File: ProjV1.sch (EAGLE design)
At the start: 24 parts, among them IC1 CD4007UBM, IC2 CD4007UBM, IC3 CD4007UBM, U1 MIC5504-3.3YM5-T5, U2 MCP2200-I/SS, U3 ATMEGA328PB-AU, U4 EN11-HSM1BF20, Y1 CSTNE12M0G55A000R0

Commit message: Updated Schematic
Fixed usb, made power source changes, got rid of missing part error relayed out board
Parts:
- removed CN1: (no value), adafruit:USBMINIB
- added R1, R2, R3, R4: 10k, rcl:R-US_R0805
- added T5, T6: (no value), zetex:NMOSSOT23
- added USB1: C77238, usbFromLCSC:C77238
- U2: value MCP2200-I/SS -> MCP2200-I/MQ; device MCP2200-I_SS:MCP2200-I/SS -> MCP2200-I_MQ:MCP2200-I/MQ
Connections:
- net RX/TX renamed N$10
- net TX/RX renamed N$11
- removed net N$8: CN1.ID
- new net N$16: R2.1, T5.S, U$1.SDA
- new net N$19: R4.1, T6.S, U$1.SCL
- new net N$7: C1.1, U2.VUSB
- net +3V3: now also R2.2, R4.2, T5.G, T6.G; no longer C1.1, ISP1.VCC, U2.VDD, U2.VUSB, U3.AVCC, U3.VCC
- net +5V: now also ISP1.VCC, R1.2, R3.2, U2.VDD, U3.AVCC, U3.VCC, USB1.VBUS; no longer CN1.VBUS
- net 0: now also U2.!RST, U2.EXP, USB1.GND, USB1.SHEILD1, USB1.SHEILD2, USB1.SHEILD3, USB1.SHEILD4; no longer CN1.GND
- net C4: now also IC2.Q2_(N)_DRAIN, IC2.Q2_(P)_DRAIN; no longer IC2.Q1_(N)_DRAIN, IC2.Q1_(P)_SOURCE
- net C5: now also IC2.Q1_(N)_DRAIN, IC2.Q1_(P)_SOURCE; no longer IC2.Q2_(N)_DRAIN, IC2.Q2_(P)_DRAIN
- net D+: now also U2.GP6/RXLED, USB1.D+; no longer CN1.D+, U2.D+
- net D-: now also U2.GP7/TXLED, USB1.D-; no longer CN1.D-, U2.D-
- net LC4: now also IC2.Q2_GATES; no longer IC2.Q1_GATES
- net LC5: now also IC2.Q1_GATES; no longer IC2.Q2_GATES
- net SCL: now also R3.1, T6.D; no longer U$1.SCL
- net SDA: now also R1.1, T5.D; no longer U$1.SDA
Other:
- moved on the sheet: C1, T1, T2, T3, T4

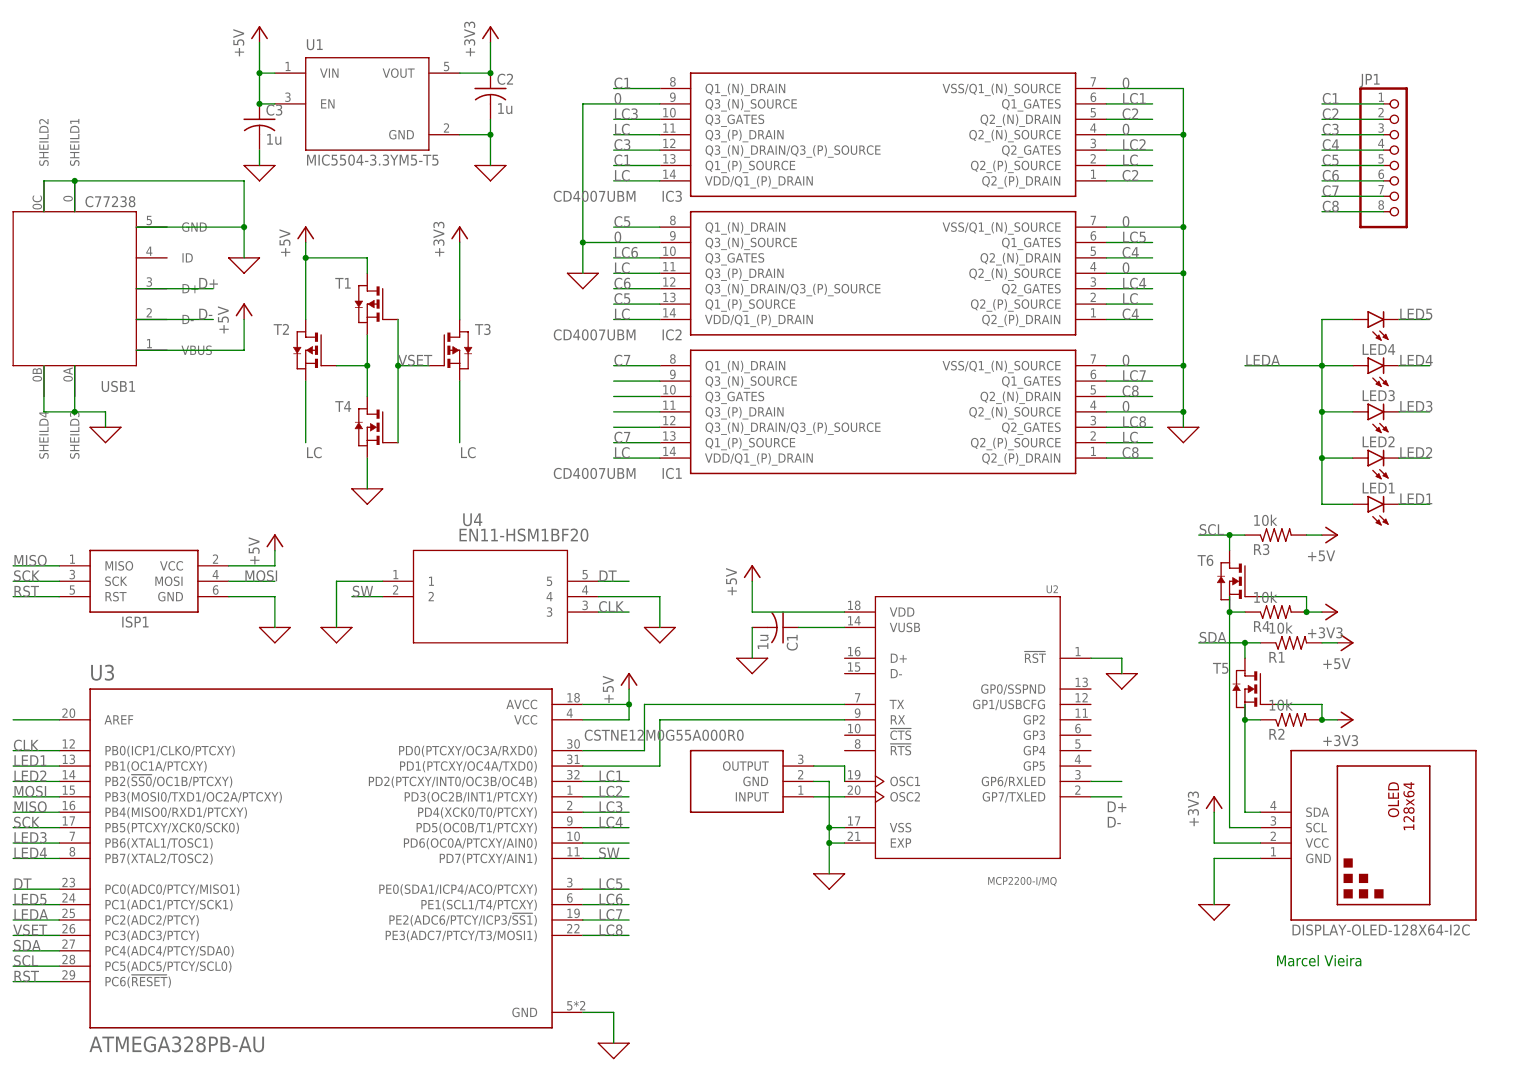
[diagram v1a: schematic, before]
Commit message: Added copies of old versions
Updated version numbers and add old versions for comparison and report writing
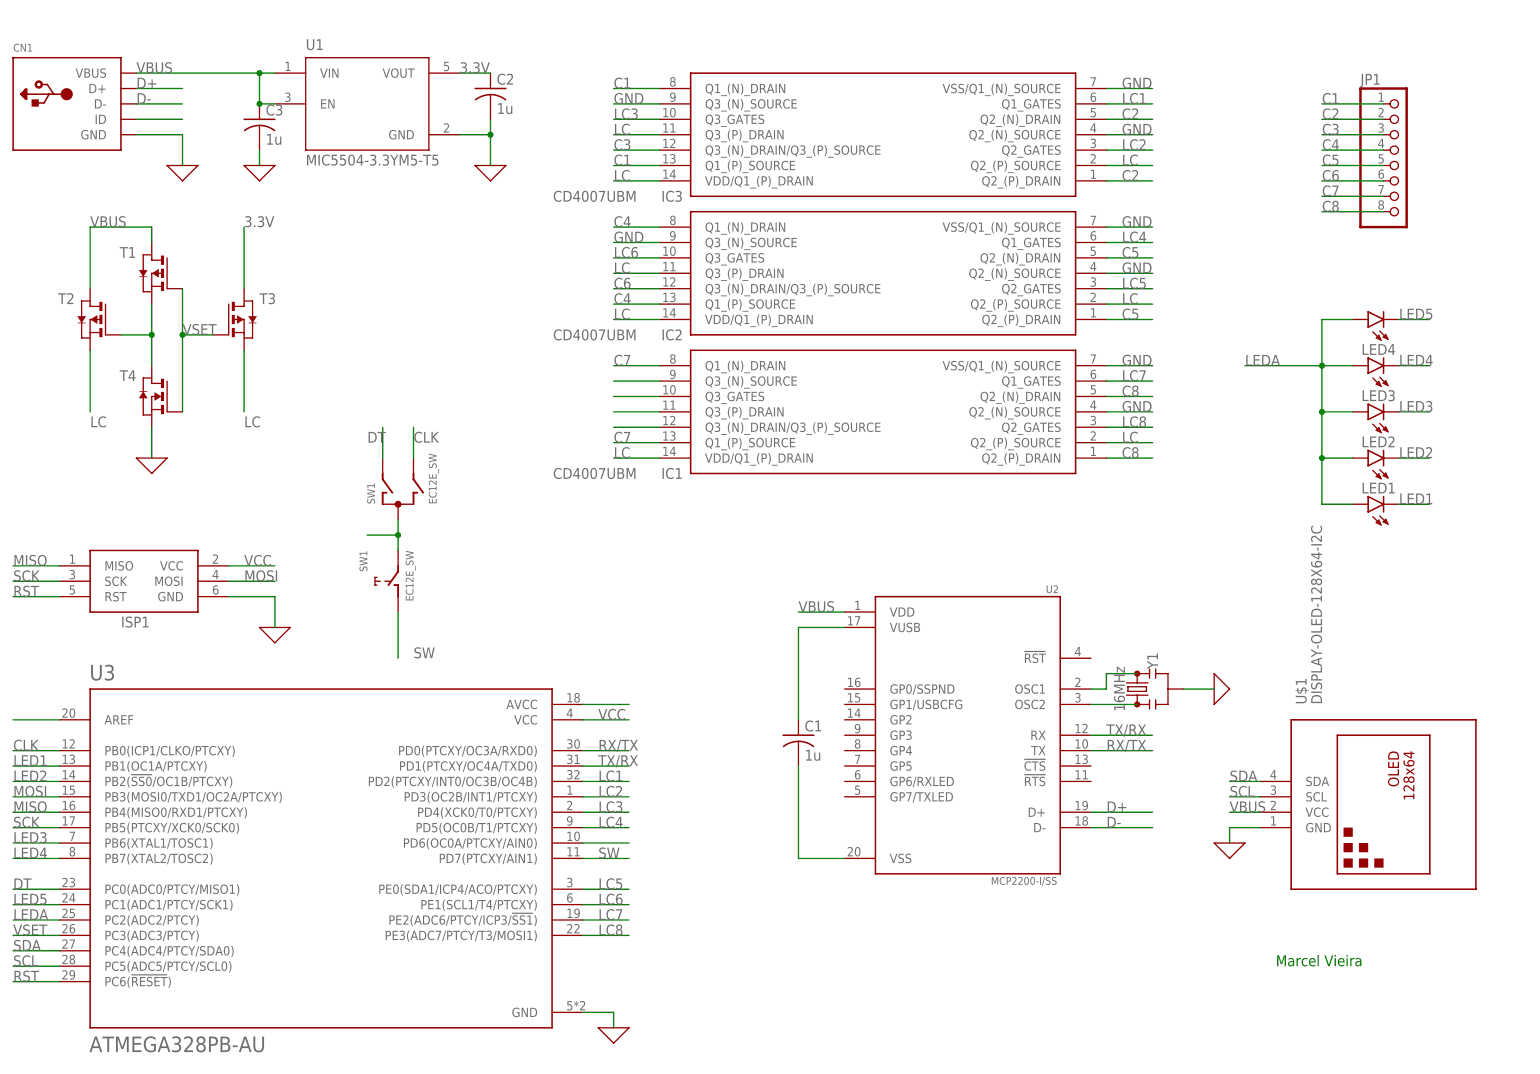
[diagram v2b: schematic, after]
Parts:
- removed R1, R2, R3, R4: 10k, rcl:R-US_R0805
- removed T5, T6: (no value), zetex:NMOSSOT23
- removed U4: EN11-HSM1BF20, EN11-HSM1BF20:EN11-HSM1BF20
- removed USB1: C77238, usbFromLCSC:C77238
- added CN1: (no value), adafruit:USBMINIB
- added SW1: EC12E_SW, switch-alps:EC12E_SW
- U2: value MCP2200-I/MQ -> MCP2200-I/SS; device MCP2200-I_MQ:MCP2200-I/MQ -> MCP2200-I_SS:MCP2200-I/SS
- Y1: value CSTNE12M0G55A000R0 -> 16MHz; device CSTNE12M0G55A000R0:CSTNE12M0G55A000R0 -> SparkFun-Clocks:RESONATOR-16MHZSMD_3.2X1.3
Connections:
- net N$10 renamed RX/TX
- net N$11 renamed TX/RX
- removed net +3V3: C2.1, R2.2, R4.2, T3.D, T5.G, T6.G, U$1.VCC, U1.VOUT
- removed net +5V: C3.1, ISP1.VCC, R1.2, R3.2, T1.D, T2.D, U1.EN, U1.VIN, U2.VDD, U3.AVCC, U3.VCC, USB1.VBUS
- removed net N$16: R2.1, T5.S, U$1.SDA
- removed net N$19: R4.1, T6.S, U$1.SCL
- new net 3.3V: C2.1, T3.D, U1.VOUT
- new net GND: IC1.Q2_(N)_SOURCE, IC1.VSS/Q1_(N)_SOURCE, IC2.Q2_(N)_SOURCE, IC2.Q3_(N)_SOURCE, IC2.VSS/Q1_(N)_SOURCE, IC3.Q2_(N)_SOURCE, IC3.Q3_(N)_SOURCE, IC3.VSS/Q1_(N)_SOURCE
- new net N$11: C1.2, U2.VSS
- new net N$31: U3.AVCC
- new net N$7: SW1G$1.C, SW1G$2.2
- new net N$8: CN1.ID
- new net VBUS: C3.1, CN1.VBUS, T1.D, T2.D, U$1.VCC, U1.EN, U1.VIN, U2.VDD
- new net VCC: ISP1.VCC, U3.VCC
- net 0: now also CN1.GND, Y1.2; no longer C1.2, IC1.Q2_(N)_SOURCE, IC1.VSS/Q1_(N)_SOURCE, IC2.Q2_(N)_SOURCE, IC2.Q3_(N)_SOURCE, IC2.VSS/Q1_(N)_SOURCE, IC3.Q2_(N)_SOURCE, IC3.Q3_(N)_SOURCE, IC3.VSS/Q1_(N)_SOURCE, U2.!RST, U2.EXP, U2.VSS, U4.1, U4.4, USB1.GND, USB1.SHEILD1, USB1.SHEILD2, USB1.SHEILD3, USB1.SHEILD4, Y1.GND
- net C4: now also IC2.Q1_(N)_DRAIN, IC2.Q1_(P)_SOURCE; no longer IC2.Q2_(N)_DRAIN, IC2.Q2_(P)_DRAIN
- net C5: now also IC2.Q2_(N)_DRAIN, IC2.Q2_(P)_DRAIN; no longer IC2.Q1_(N)_DRAIN, IC2.Q1_(P)_SOURCE
- net CLK: now also SW1G$1.B; no longer U4.3
- net D+: now also CN1.D+, U2.D+; no longer U2.GP6/RXLED, USB1.D+
- net D-: now also CN1.D-, U2.D-; no longer U2.GP7/TXLED, USB1.D-
- net DT: now also SW1G$1.A; no longer U4.5
- net LC4: now also IC2.Q1_GATES; no longer IC2.Q2_GATES
- net LC5: now also IC2.Q2_GATES; no longer IC2.Q1_GATES
- net N$14: now also Y1.3; no longer Y1.INPUT
- net N$6: now also Y1.1; no longer Y1.OUTPUT
- net SCL: now also U$1.SCL; no longer R3.1, T6.D
- net SDA: now also U$1.SDA; no longer R1.1, T5.D
- net SW: now also SW1G$2.1; no longer U4.2
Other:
- moved on the sheet: C1, T1, T2, T3, T4
